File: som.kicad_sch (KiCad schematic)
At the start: 38 parts, among them J10 5051101097, T2 BSS138APW, T4 BSS138APW, T5 BSS138APW

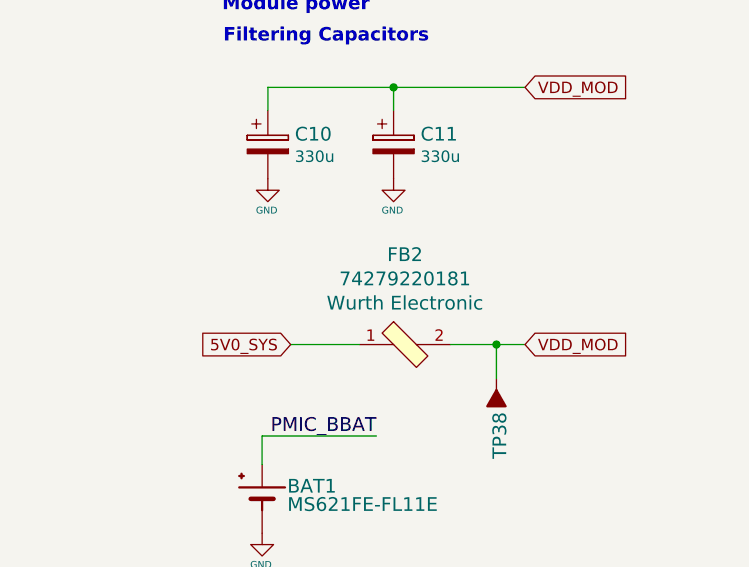
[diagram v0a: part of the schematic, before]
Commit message: Update local libraries
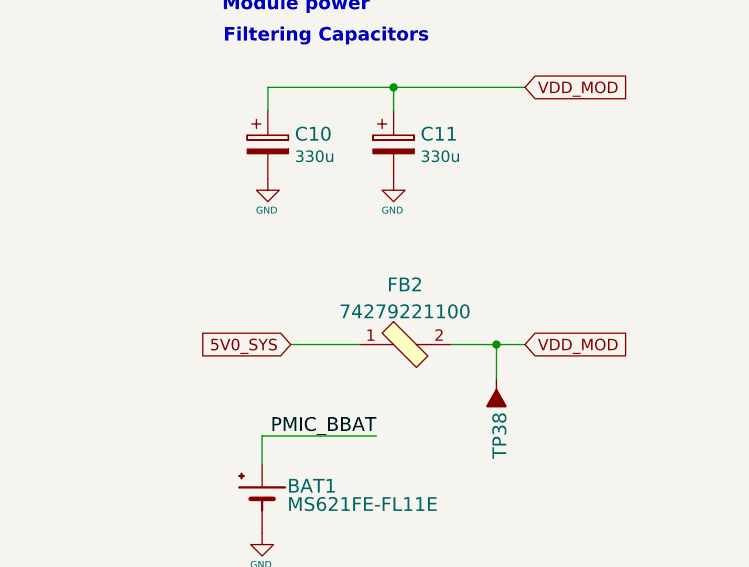
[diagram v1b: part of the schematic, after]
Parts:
- removed FB2: 74279220181, jetson-nano-baseboard-footprints:0805-res, symbol jetson-nano-baseboard:74279220181
- added FB2: 74279221100, jetson-nano-baseboard-footprints:1206-res, symbol jetson-nano-baseboard:74279221100
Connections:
- net 5V0_SYS: now also FB2.1
- net VDD_MOD: now also FB2.2

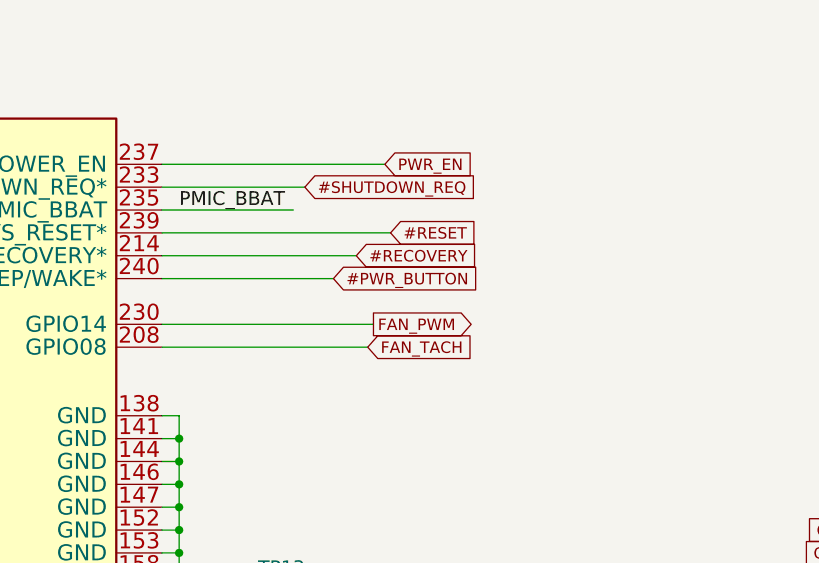
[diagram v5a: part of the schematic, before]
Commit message: Add #RESET pull-down
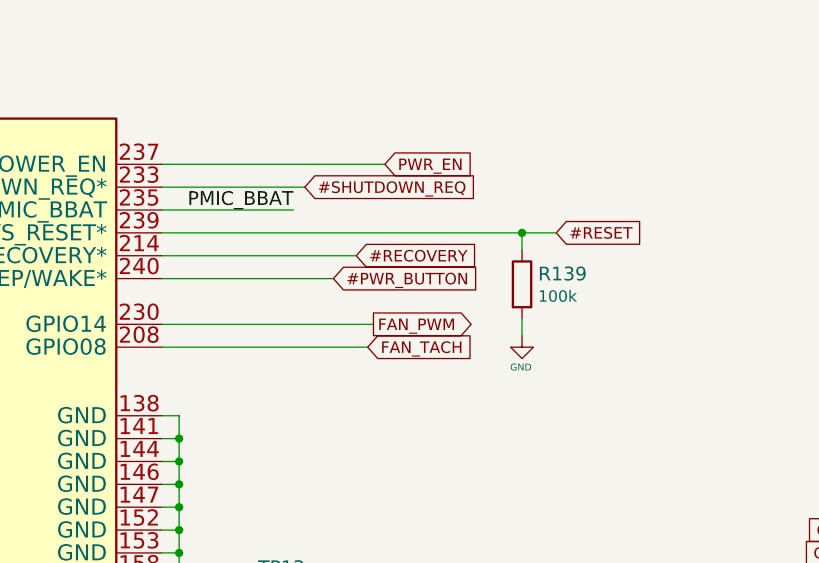
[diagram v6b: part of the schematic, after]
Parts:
- added R139: R_100k_0402, jetson-nano-baseboard-footprints:0402-res, symbol jetson-nano-baseboard:R_100k_0402
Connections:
- net #RESET: now also R139.1
- net GND: now also R139.2
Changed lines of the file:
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@@
   (junction (at 383.54 234.315) (diameter 0) (color 0 0 0 0)
   )
+  (junction (at 137.795 34.925) (diameter 0) (color 0 0 0 0)
+  )
   (junction (at 99.695 128.905) (diameter 0) (color 0 0 0 0)
   )
@@
     (stroke (width 0) (type default) (color 0 0 0 0))
   )
+  (wire (pts (xy 137.795 34.925) (xy 137.795 36.83))
+    (stroke (width 0) (type default) (color 0 0 0 0))
+  )
   (wire (pts (xy 191.135 203.835) (xy 205.74 203.835))
     (stroke (width 0) (type default) (color 0 0 0 0))
@@
     (stroke (width 0) (type default) (color 0 0 0 0))
   )
+  (wire (pts (xy 137.795 34.925) (xy 141.605 34.925))
+    (stroke (width 0) (type default) (color 0 0 0 0))
+  )
   (wire (pts (xy 205.74 186.055) (xy 192.405 186.055))
     (stroke (width 0) (type default) (color 0 0 0 0))
@@
     (stroke (width 0) (type default) (color 0 0 0 0))
   )
-  (wire (pts (xy 97.79 34.925) (xy 123.19 34.925))
+  (wire (pts (xy 97.79 34.925) (xy 137.795 34.925))
     (stroke (width 0) (type default) (color 0 0 0 0))
   )
@@
     (stroke (width 0) (type default) (color 0 0 0 0))
   )
+  (wire (pts (xy 137.795 44.45) (xy 137.795 46.355))
+    (stroke (width 0) (type default) (color 0 0 0 0))
+  )
   (wire (pts (xy 46.99 111.125) (xy 43.815 111.125))
     (stroke (width 0) (type default) (color 0 0 0 0))
@@
     (effects (font (size 1.524 1.524)) (justify left bottom))
   )
-  (label "PMIC_BBAT" (at 99.695 32.385 0)
-    (effects (font (size 1.524 1.524)) (justify left bottom))
+  (label "PMIC_BBAT" (at 112.395 32.385 180)
+    (effects (font (size 1.524 1.524)) (justify right bottom))
   )
   (label "PCIE1_TX0_N" (at 267.335 47.625 0)
@@
     )
   )
-  (global_label "#RESET" (shape input) (at 123.19 34.925 0) (fields_autoplaced)
+  (global_label "#RESET" (shape input) (at 141.605 34.925 0) (fields_autoplaced)
     (effects (font (size 1.27 1.27)) (justify left))
-    (property "Intersheet References" "${INTERSHEET_REFS}" (id 0) (at 0 0 0)
+    (property "Intersheet References" "${INTERSHEET_REFS}" (id 0) (at 18.415 0 0)
       (effects (font (size 1.27 1.27)) hide)
     )
@@
     (pin "2")
   )
+  (symbol (lib_id "jetson-nano-baseboard:R_100k_0402") (at 137.795 40.64 270) (unit 1)
+    (in_bom yes) (on_board yes)
+    (property "Reference" "R139" (id 0) (at 139.573 39.497 90)
+      (effects (font (size 1.524 1.524)) (justify left))
+    )
+    (property "Value" "R_100k_0402" (id 1) (at 133.985 40.64 0)
+      (effects (font (size 1.524 1.524)) hide)
+    )
+    (property "Footprint" "jetson-nano-baseboard-footprints:0402-res" (id 2) (at 142.875 45.72 0)
+      (effects (font (size 1.524 1.524)) (justify left) hide)
+    )
+    (property "Datasheet" "" (id 3) (at 137.795 40.64 0)
+      (effects (font (size 1.27 1.27)) hide)
+    )
+    (property "Manufacturer" "VISHAY" (id 4) (at 147.955 45.72 0)
+      (effects (font (size 1.524 1.524)) (justify left) hide)
+    )
+    (property "MPN" "CRCW0402100KFKEDHP" (id 5) (at 145.415 45.72 0)
+      (effects (font (size 1.524 1.524)) (justify left) hide)
+    )
+    (property "Val" "100k" (id 6) (at 139.573 41.9862 90)
+      (effects (font (size 1.27 1.27)) (justify left))
+    )
+    (pin "1")
+    (pin "2")
+  )
   (symbol (lib_id "jetson-nano-baseboard:74279221100") (at 365.76 61.595 0) (unit 1)
     (in_bom yes) (on_board yes) (fields_autoplaced)
@@
     (pin "2")
   )
+  (symbol (lib_id "jetson-nano-baseboard:GND") (at 137.795 46.355 0) (unit 1)
+    (in_bom yes) (on_board yes)
+    (property "Reference" "#GND_011" (id 0) (at 137.795 46.355 0)
+      (effects (font (size 0.508 0.508)) hide)
+    )
+    (property "Value" "GND" (id 1) (at 137.668 49.8602 0)
+      (effects (font (size 0.762 0.762)))
+    )
+    (property "Footprint" "" (id 2) (at 137.795 46.355 0)
+      (effects (font (size 1.778 1.778)) hide)
+    )
+    (property "Datasheet" "" (id 3) (at 137.795 46.355 0)
+      (effects (font (size 1.778 1.778)) hide)
+    )
+    (pin "1")
+  )
 )

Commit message: Standardize components
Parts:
- removed J10: 5051101097, jetson-nano-baseboard-footprints:5051101097, symbol jetson-nano-baseboard:5051101097
- removed R113: 100k, jetson-nano-baseboard-footprints:0402, symbol jetson-nano-baseboard:R_100k_0402
- removed REC1, RST1, USR1: ~, jetson-nano-baseboard-footprints:TL3340AF160QG, symbol jetson-nano-baseboard:TL3340AF160QG
- added J10: Conn_FFC_Molex_5051101097, antmicro-footprints:Conn_FFC_Molex_5051101097, symbol antmicroFCCConnectors:Conn_FFC_Molex_5051101097
- added R113: R_100k_0402, antmicro-footprints:R_0402_1005Metric, symbol antmicroResistors0402:R_100k_0402
- added REC1, RST1, USR1: SW_TL3340AF160QG, antmicro-footprints:SW_TL3340AF160QG, symbol antmicroPushbuttonSwitches:SW_TL3340AF160QG
- BAT1: footprint jetson-nano-baseboard-footprints:MS621FE-FL11E -> antmicro-footprints:MS621FE-FL11E; symbol jetson-nano-baseboard:battery -> antmicroBatteryHoldersClipsContacts:Battery_Holder_MS621FE-FL11E; Author (none) -> Antmicro; License (none) -> Apache-2.0
- BOOT1, PWR1, USER1: footprint jetson-nano-baseboard-footprints:LED0603 -> antmicro-footprints:LED_0603_1608Metric_G; symbol jetson-nano-baseboard:LED -> antmicroLEDIndicationDiscrete:LED_G_0603_LG_L29K-G2J1-24-Z; Author (none) -> Antmicro; License (none) -> Apache-2.0; MPN KPT-1608SGC -> LG L29K-G2J1-24-Z; Manufacturer Kingbright -> Osram
- C10, C11: footprint jetson-nano-baseboard-footprints:KEMET_B -> antmicro-footprints:KEMET_B; symbol jetson-nano-baseboard:C_330u_KEMET_B -> antmicroCapacitorspol:C_330u_KEMET_B; Author (none) -> Antmicro; License (none) -> Apache-2.0
- FB2: value 74279221100 -> FB_10Z_10A_1206; footprint jetson-nano-baseboard-footprints:1206-res -> antmicro-footprints:FB_1206_3216Metric; symbol jetson-nano-baseboard:74279221100 -> antmicroFerriteBeadsandChips:FB_10Z_10A_1206; Author (none) -> Antmicro; License (none) -> Apache-2.0; Manufacturer Wurth Electronic -> Würth Elektronik
- M1: value ~ -> Jetson-Nano-new-release; footprint jetson-nano-baseboard-footprints:jetson-nano-connector -> antmicro-footprints:TE_2309413; symbol jetson-nano-baseboard:Jetson-Nano-new-release -> antmicroSoMConnectors:Jetson-Nano-new-release; Author (none) -> Antmicro; License (none) -> Apache-2.0; Manufacturer TE -> TE Connectivity
- M2: value ~ -> jetson-nano-module; footprint jetson-nano-baseboard-footprints:jetson-nano-module -> antmicro-footprints:jetson-nano-module-5.2H; symbol jetson-nano-baseboard:Jetson-Nano-Module-model -> antmicroModules:jetson-nano-module; Author (none) -> Antmicro; License (none) -> Apache-2.0; MPN 900-13448-0020-000 -> 945-13541-0000-0000; Manufacturer Nvidia -> NVIDIA
- R111, R14, R97: footprint jetson-nano-baseboard-footprints:0402-res -> antmicro-footprints:R_0402_1005Metric; symbol jetson-nano-baseboard:R_470R_0402 -> antmicroResistors0402:R_470R_0402; Author (none) -> Antmicro; License (none) -> Apache-2.0; MPN CRCW0402470RFKED -> CR0402-FX-4700GLF; Manufacturer VISHAY -> Bourns; Tolerance (none) -> 1%
- R112, R139: footprint jetson-nano-baseboard-footprints:0402-res -> antmicro-footprints:R_0402_1005Metric; symbol jetson-nano-baseboard:R_100k_0402 -> antmicroResistors0402:R_100k_0402; Author (none) -> Antmicro; License (none) -> Apache-2.0; MPN CRCW0402100KFKEDHP -> CR0402-FX-1003GLF; Manufacturer VISHAY -> Bourns; Tolerance (none) -> 1%
- SP1, SP2, SP3, SP4, SP5, SP6: footprint jetson-nano-baseboard-footprints:M2.5-6mm -> antmicro-footprints:Spacer_SMD_M2.5_H6mm_Wurth_9774060151; symbol jetson-nano-baseboard:SPACER -> antmicroMechanicalParts:Spacer_H6mm_9774060151; Author (none) -> Antmicro; License (none) -> Apache-2.0; Manufacturer Wurth Elektronik -> Würth Elektronik
- T2, T4, T5: value BSS138APW -> BSS138PW; footprint jetson-nano-baseboard-footprints:SC70-3 -> antmicro-footprints:SC70-3; symbol jetson-nano-baseboard:BSS138APW -> antmicroTransistorsFETsMOSFETsSingle:BSS138PW; Author (none) -> Antmicro; License (none) -> Apache-2.0; Manufacturer ON Semiconductor -> Nexperia
- TP13, TP14, TP23, TP24, TP27, TP28, TP29, TP31, TP37, TP38, TP39: value ~ -> TP_1.5mm_SMD; footprint jetson-nano-baseboard-footprints:TP-R-1.5 -> antmicro-footprints:TP_SMD_1.5mm; symbol jetson-nano-baseboard:Testpad -> antmicroTestPoints:TP_1.5mm_SMD; Author (none) -> Antmicro; License (none) -> Apache-2.0
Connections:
- net #RECOVERY: now also REC1.2
- net #RESET: now also RST1.2
- net 3V3_SYS: now also J10.1
- net 5V0_SYS: now also R111.1, R14.1, R97.1; no longer R111.2, R14.2, R97.2
- net GND: now also J10.10, R113.1, REC1.1, REC1.3, REC1.SH, RST1.1, RST1.3, RST1.SH, USR1.1, USR1.3, USR1.SH
- net PCIE1_CLKREQ: now also J10.3
- net PCIE1_CLK_N: now also J10.5
- net PCIE1_CLK_P: now also J10.4
- net PCIE1_RST: now also J10.2
- net PCIE1_RX0_N: now also J10.9
- net PCIE1_RX0_P: now also J10.8
- net PCIE1_TX0_N: now also J10.7
- net PCIE1_TX0_P: now also J10.6
- net USR_BUTTON: now also USR1.2
- net USR_LED: now also R113.2
- net at USER1.1: now also R111.2; no longer R111.1
- net at PWR1.1: now also R97.2; no longer R97.1
- net at BOOT1.1: now also R14.2; no longer R14.1
- net BT_M2_EN: no longer names the net of M1.126 (GPIO03)
- net BT_M2_WAKE_AP: no longer names the net of M1.124 (GPIO02)
- net USB2_D_N: no longer names the net of M1.121 (USB2_D_N)
- net USB2_D_P: no longer names the net of M1.123 (USB2_D_P)
- net ~{SD_VCC_EN}: no longer names the net of M1.211 (GPIO09)
- no-connect marks 1 -> 42
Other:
- moved on the sheet: M1C, M1D, M1F, M1G, R111, R112, R139, R14, R97
